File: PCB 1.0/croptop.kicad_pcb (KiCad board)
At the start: 4 copper layers, 115.6 x 45.7 mm, 241 parts, among them J1 PICKit Header, J2 USB_A, J3 5V USB, J4 4-1734839-0, J5 Terminal Block, J6 DNP, J7 DNP, SW1 BTNA, SW2 BTNA, U1 PIC32MX795F512L, U10 AD7799, U11 74HCT125D, U12 Si7006-A20, U13 UCAM-M8Q, U14 W25N01GV, U15 LIS3DH, U16 PUSBM5V5X4, U17 DT6250-06MR-13, U18 PUSBM5V5X4, U2 REG71055, U3 FAN5333BSX, U4 MIC23050, U5 TC1014, U6 FT812Q, U8 74HCT125D, U9 DRV8872, Y1 CXO, Y2 12MHz

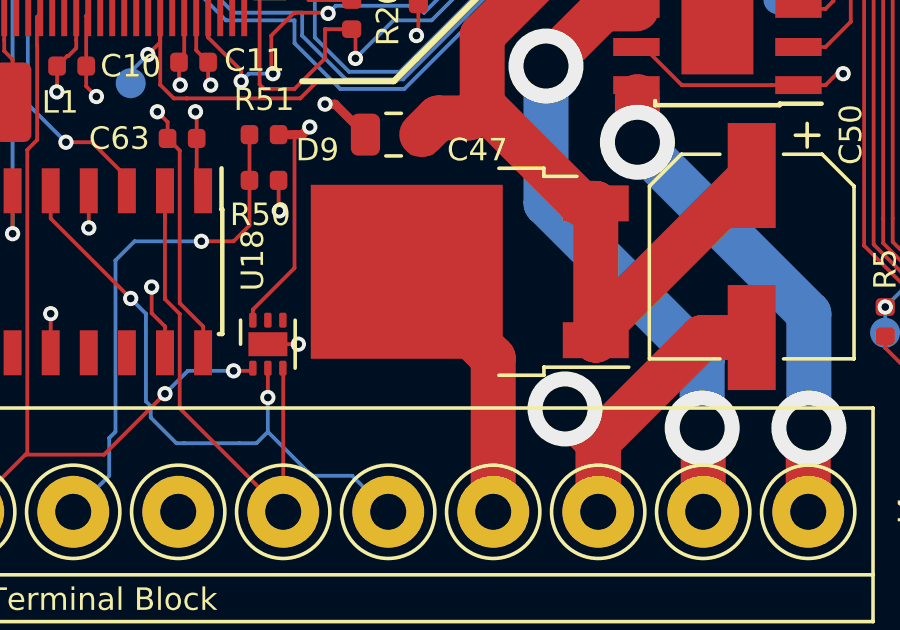
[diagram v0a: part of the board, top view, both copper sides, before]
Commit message: New microcontroller pinout
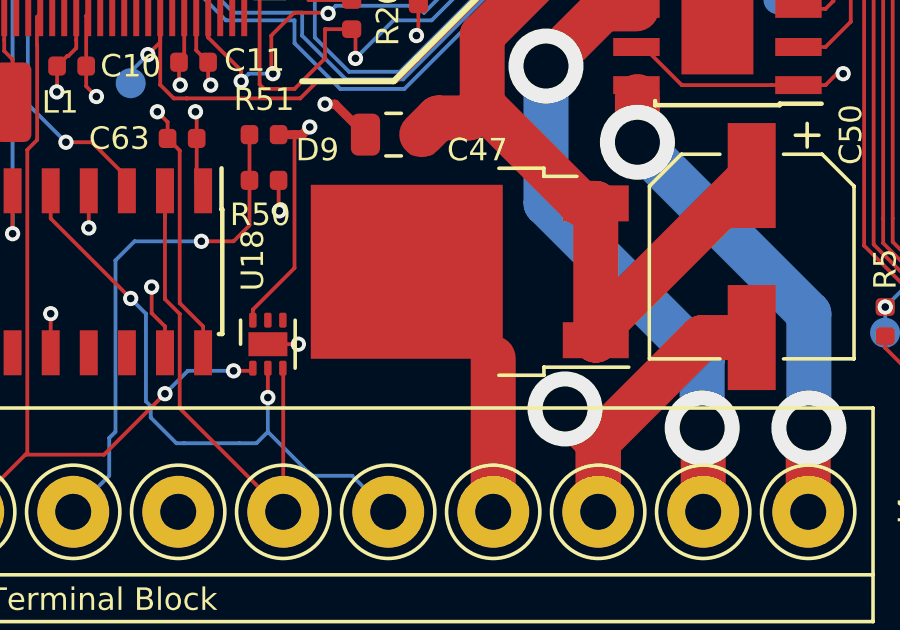
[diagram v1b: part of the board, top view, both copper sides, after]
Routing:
- net DRV_BAT: track 9.19 -> 5.12 mm
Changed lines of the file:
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@@
     (thickness 1.6)
     (drawings 83)
-    (tracks 2754)
+    (tracks 2753)
     (zones 0)
     (modules 241)
@@
     (0 F.Cu signal)
     (1 Gnd.Cu power hide)
-    (2 Vdd.Cu power)
+    (2 Vdd.Cu power hide)
     (31 B.Cu signal)
     (32 B.Adhes user hide)
@@
     (34 B.Paste user hide)
     (35 F.Paste user hide)
-    (36 B.SilkS user)
-    (37 F.SilkS user)
+    (36 B.SilkS user hide)
+    (37 F.SilkS user hide)
     (38 B.Mask user hide)
     (39 F.Mask user hide)
@@
   (segment (start 170.942 139.169) (end 170.965 139.192) (width 0.127) (layer F.Cu) (net 25))
   (segment (start 170.942 136.5735) (end 170.942 139.169) (width 0.127) (layer F.Cu) (net 25))
-  (segment (start 117.875 132.675) (end 114.994 129.794) (width 1.5) (layer F.Cu) (net 26))
   (segment (start 117.875 137.795) (end 117.875 132.675) (width 1.5) (layer F.Cu) (net 26))
   (segment (start 162.4075 115.547) (end 162.8925 115.062) (width 0.127) (layer F.Cu) (net 27))
